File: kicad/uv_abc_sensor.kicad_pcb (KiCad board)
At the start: 2 copper layers, 25.4 x 17.8 mm, 23 parts, among them J1 Conn_01x04, J2 Conn_01x04, M1 MountingHole_2.5mm_Pad, M2 MountingHole_2.5mm_Pad, M3 MountingHole_2.5mm_Pad, M4 MountingHole_2.5mm_Pad, Q1 BSS138, Q2 BSS138, U1 AS7331, U2 AP2112K-3.3

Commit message: More work on layout.
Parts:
- moved C3 5.03 mm to (56.3, 55.8), turned to -90 degrees
- moved C4 2.55 mm to (59.3, 54.3), turned to 180 degrees
- moved U2 1.36 mm to (59.3, 56.8), turned to 0 degrees
- moved R7 0.51 mm to (61.2, 59.9)
- moved J1 0.13 mm to (53.5, 59.7)
- moved J2 0.13 mm to (73.6, 59.6)
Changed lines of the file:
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@@
   )
   (footprint "BOOMELE_SH_SMD:BOOMELE_SMD_SH_4PIN_RT" (layer "F.Cu")
-    (at 73.688 59.58 -90)
+    (at 73.561 59.58 -90)
     (property "Sheetfile" "uv_abc_sensor.kicad_sch")
     (property "Sheetname" "")
@@
   )
   (footprint "Capacitor_SMD:C_0402_1005Metric" (layer "F.Cu")
-    (at 61.534 55.4765 90)
+    (at 59.2755 54.29 180)
     (descr "Capacitor SMD 0402 (1005 Metric), square (rectangular) end terminal, IPC_7351 nominal, (Body size source: IPC-SM-782 page 76, https://www.pcb-3d.com/wordpress/wp-content/uploads/ipc-sm-782a_amendment_1_and_2.pdf), generated with kicad-footprint-generator")
     (tags "capacitor")
@@
     (property "ki_keywords" "cap capacitor")
     (attr smd)
-    (fp_text reference "C4" (at 0 -1.16 90) (layer "F.SilkS") hide
-        (effects (font (size 1 1) (thickness 0.15)))
-    )
-    (fp_text value "10uF" (at 0 1.16 90) (layer "F.Fab") hide
-        (effects (font (size 1 1) (thickness 0.15)))
-    )
-    (fp_text user "${REFERENCE}" (at 0 0 90) (layer "F.Fab")
+    (fp_text reference "C4" (at 0 -1.16) (layer "F.SilkS") hide
+        (effects (font (size 1 1) (thickness 0.15)))
+    )
+    (fp_text value "10uF" (at 0 1.16) (layer "F.Fab") hide
+        (effects (font (size 1 1) (thickness 0.15)))
+    )
+    (fp_text user "${REFERENCE}" (at 0 0) (layer "F.Fab")
         (effects (font (size 0.25 0.25) (thickness 0.04)))
     )
@@
     (fp_line (start 0.5 0.25) (end -0.5 0.25)
       (stroke (width 0.1) (type solid)) (layer "F.Fab"))
-    (pad "1" smd roundrect (at -0.48 0 90) (size 0.56 0.62) (layers "F.Cu" "F.Paste" "F.Mask") (roundrect_rratio 0.25)
+    (pad "1" smd roundrect (at -0.48 0 180) (size 0.56 0.62) (layers "F.Cu" "F.Paste" "F.Mask") (roundrect_rratio 0.25)
       (net 1 "+3.3V") (pintype "passive"))
-    (pad "2" smd roundrect (at 0.48 0 90) (size 0.56 0.62) (layers "F.Cu" "F.Paste" "F.Mask") (roundrect_rratio 0.25)
+    (pad "2" smd roundrect (at 0.48 0 180) (size 0.56 0.62) (layers "F.Cu" "F.Paste" "F.Mask") (roundrect_rratio 0.25)
       (net 2 "GND") (pintype "passive"))
     (model "${KICAD6_3DMODEL_DIR}/Capacitor_SMD.3dshapes/C_0402_1005Metric.wrl"
@@
   )
   (footprint "Resistor_SMD:R_0402_1005Metric" (layer "F.Cu")
-    (at 60.706 59.946 90)
+    (at 61.214 59.944 90)
     (descr "Resistor SMD 0402 (1005 Metric), square (rectangular) end terminal, IPC_7351 nominal, (Body size source: IPC-SM-782 page 72, https://www.pcb-3d.com/wordpress/wp-content/uploads/ipc-sm-782a_amendment_1_and_2.pdf), generated with kicad-footprint-generator")
     (tags "resistor")
@@
     (property "ki_keywords" "R res resistor")
     (attr smd)
-    (fp_text reference "R7" (at 0 -1.17 90) (layer "F.SilkS")
-        (effects (font (size 1 1) (thickness 0.15)))
-    )
-    (fp_text value "10k" (at 0 1.17 90) (layer "F.Fab")
+    (fp_text reference "R7" (at 0 -1.17 90) (layer "F.SilkS") hide
+        (effects (font (size 1 1) (thickness 0.15)))
+    )
+    (fp_text value "10k" (at 0 1.17 90) (layer "F.Fab") hide
         (effects (font (size 1 1) (thickness 0.15)))
     )
@@
   )
   (footprint "BOOMELE_SH_SMD:BOOMELE_SMD_SH_4PIN_RT" (layer "F.Cu")
-    (at 53.34 59.69 90)
+    (at 53.467 59.69 90)
     (property "Sheetfile" "uv_abc_sensor.kicad_sch")
     (property "Sheetname" "")
@@
   )
   (footprint "Capacitor_SMD:C_0402_1005Metric" (layer "F.Cu")
-    (at 59.982 52.4565 180)
+    (at 56.2555 55.842 -90)
     (descr "Capacitor SMD 0402 (1005 Metric), square (rectangular) end terminal, IPC_7351 nominal, (Body size source: IPC-SM-782 page 76, https://www.pcb-3d.com/wordpress/wp-content/uploads/ipc-sm-782a_amendment_1_and_2.pdf), generated with kicad-footprint-generator")
     (tags "capacitor")
@@
     (property "ki_keywords" "cap capacitor")
     (attr smd)
-    (fp_text reference "C3" (at 0 -1.16) (layer "F.SilkS") hide
-        (effects (font (size 1 1) (thickness 0.15)))
-    )
-    (fp_text value "10uF" (at 0 1.16) (layer "F.Fab") hide
-        (effects (font (size 1 1) (thickness 0.15)))
-    )
-    (fp_text user "${REFERENCE}" (at 0 0) (layer "F.Fab")
+    (fp_text reference "C3" (at 0 -1.16 -270) (layer "F.SilkS") hide
+        (effects (font (size 1 1) (thickness 0.15)))
+    )
+    (fp_text value "10uF" (at 0 1.16 -270) (layer "F.Fab") hide
+        (effects (font (size 1 1) (thickness 0.15)))
+    )
+    (fp_text user "${REFERENCE}" (at 0 0 -270) (layer "F.Fab")
         (effects (font (size 0.25 0.25) (thickness 0.04)))
     )
@@
     (fp_line (start 0.5 0.25) (end -0.5 0.25)
       (stroke (width 0.1) (type solid)) (layer "F.Fab"))
-    (pad "1" smd roundrect (at -0.48 0 180) (size 0.56 0.62) (layers "F.Cu" "F.Paste" "F.Mask") (roundrect_rratio 0.25)
+    (pad "1" smd roundrect (at -0.48 0 270) (size 0.56 0.62) (layers "F.Cu" "F.Paste" "F.Mask") (roundrect_rratio 0.25)
       (net 3 "VCC") (pintype "passive"))
-    (pad "2" smd roundrect (at 0.48 0 180) (size 0.56 0.62) (layers "F.Cu" "F.Paste" "F.Mask") (roundrect_rratio 0.25)
+    (pad "2" smd roundrect (at 0.48 0 270) (size 0.56 0.62) (layers "F.Cu" "F.Paste" "F.Mask") (roundrect_rratio 0.25)
       (net 2 "GND") (pintype "passive"))
     (model "${KICAD6_3DMODEL_DIR}/Capacitor_SMD.3dshapes/C_0402_1005Metric.wrl"
@@
   )
   (footprint "Package_TO_SOT_SMD:SOT-23-5" (layer "F.Cu")
-    (at 58.994 55.5045 -90)
+    (at 59.3035 56.83)
     (descr "SOT, 5 Pin (https://www.jedec.org/sites/default/files/docs/Mo-178c.PDF variant AA), generated with kicad-footprint-generator ipc_gullwing_generator.py")
     (tags "SOT TO_SOT_SMD")
@@
     (property "ki_keywords" "linear regulator ldo fixed positive")
     (attr smd)
-    (fp_text reference "U2" (at 0 -2.4 90) (layer "F.SilkS") hide
-        (effects (font (size 1 1) (thickness 0.15)))
-    )
-    (fp_text value "AP2112K-3.3" (at 0 2.4 90) (layer "F.Fab") hide
-        (effects (font (size 1 1) (thickness 0.15)))
-    )
-    (fp_text user "${REFERENCE}" (at 0 0 90) (layer "F.Fab")
+    (fp_text reference "U2" (at 0 -2.4) (layer "F.SilkS") hide
+        (effects (font (size 1 1) (thickness 0.15)))
+    )
+    (fp_text value "AP2112K-3.3" (at 0 2.4) (layer "F.Fab") hide
+        (effects (font (size 1 1) (thickness 0.15)))
+    )
+    (fp_text user "${REFERENCE}" (at 0 0) (layer "F.Fab")
         (effects (font (size 0.4 0.4) (thickness 0.06)))
     )
@@
     (fp_line (start 0.8 1.45) (end -0.8 1.45)
       (stroke (width 0.1) (type solid)) (layer "F.Fab"))
-    (pad "1" smd roundrect (at -1.1375 -0.95 270) (size 1.325 0.6) (layers "F.Cu" "F.Paste" "F.Mask") (roundrect_rratio 0.25)
+    (pad "1" smd roundrect (at -1.1375 -0.95) (size 1.325 0.6) (layers "F.Cu" "F.Paste" "F.Mask") (roundrect_rratio 0.25)
       (net 3 "VCC") (pinfunction "VIN") (pintype "power_in"))
-    (pad "2" smd roundrect (at -1.1375 0 270) (size 1.325 0.6) (layers "F.Cu" "F.Paste" "F.Mask") (roundrect_rratio 0.25)
+    (pad "2" smd roundrect (at -1.1375 0) (size 1.325 0.6) (layers "F.Cu" "F.Paste" "F.Mask") (roundrect_rratio 0.25)
       (net 2 "GND") (pinfunction "GND") (pintype "power_in"))
-    (pad "3" smd roundrect (at -1.1375 0.95 270) (size 1.325 0.6) (layers "F.Cu" "F.Paste" "F.Mask") (roundrect_rratio 0.25)
+    (pad "3" smd roundrect (at -1.1375 0.95) (size 1.325 0.6) (layers "F.Cu" "F.Paste" "F.Mask") (roundrect_rratio 0.25)
       (net 3 "VCC") (pinfunction "EN") (pintype "input"))
-    (pad "4" smd roundrect (at 1.1375 0.95 270) (size 1.325 0.6) (layers "F.Cu" "F.Paste" "F.Mask") (roundrect_rratio 0.25)
+    (pad "4" smd roundrect (at 1.1375 0.95) (size 1.325 0.6) (layers "F.Cu" "F.Paste" "F.Mask") (roundrect_rratio 0.25)
       (net 13 "unconnected-(U2-NC-Pad4)") (pinfunction "NC") (pintype "no_connect"))
-    (pad "5" smd roundrect (at 1.1375 -0.95 270) (size 1.325 0.6) (layers "F.Cu" "F.Paste" "F.Mask") (roundrect_rratio 0.25)
+    (pad "5" smd roundrect (at 1.1375 -0.95) (size 1.325 0.6) (layers "F.Cu" "F.Paste" "F.Mask") (roundrect_rratio 0.25)
       (net 1 "+3.3V") (pinfunction "VOUT") (pintype "power_out"))
     (model "${KICAD6_3DMODEL_DIR}/Package_TO_SOT_SMD.3dshapes/SOT-23-5.wrl"
@@
     (property "ki_keywords" "R res resistor")
     (attr smd)
-    (fp_text reference "R6" (at 0 -1.17) (layer "F.SilkS")
-        (effects (font (size 1 1) (thickness 0.15)))
-    )
-    (fp_text value "10k" (at 0 1.17) (layer "F.Fab")
-        (effects (font (size 1 1) (thickness 0.15)))
-    )
+    (fp_text reference "R6" (at 0 -1.17) (layer "F.SilkS") hide
+        (effects (font (size 1 1) (thickness 0.15)))
+    )
+    (fp_text value "10k" (at 0 1.17) (layer "F.Fab") hide
+        (effects (font (size 1 1) (thickness 0.15)))
+    )

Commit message: Worked on layout and routing.
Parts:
- moved C3 3.39 mm to (59.0, 57.9), turned to 0 degrees
- moved C4 2.45 mm to (56.9, 54.9), turned to -90 degrees
- moved U2 1.97 mm to (59.4, 54.9), turned to 90 degrees
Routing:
- net VCC: track 0.00 -> 37.4 mm, vias 0 -> 5
- net +3.3V: track 0.00 -> 31.9 mm
- net GND: track 0.00 -> 28.8 mm
- net /SCL_3V3: track 0.00 -> 2.05 mm
- net /SDA_3V3: track 0.00 -> 1.87 mm
- net Net-(U1-REXT): track 0.00 -> 1.73 mm
- net Net-(JP2-A): track 0.00 -> 1.45 mm
- net Net-(JP1-A): track 0.00 -> 1.23 mm

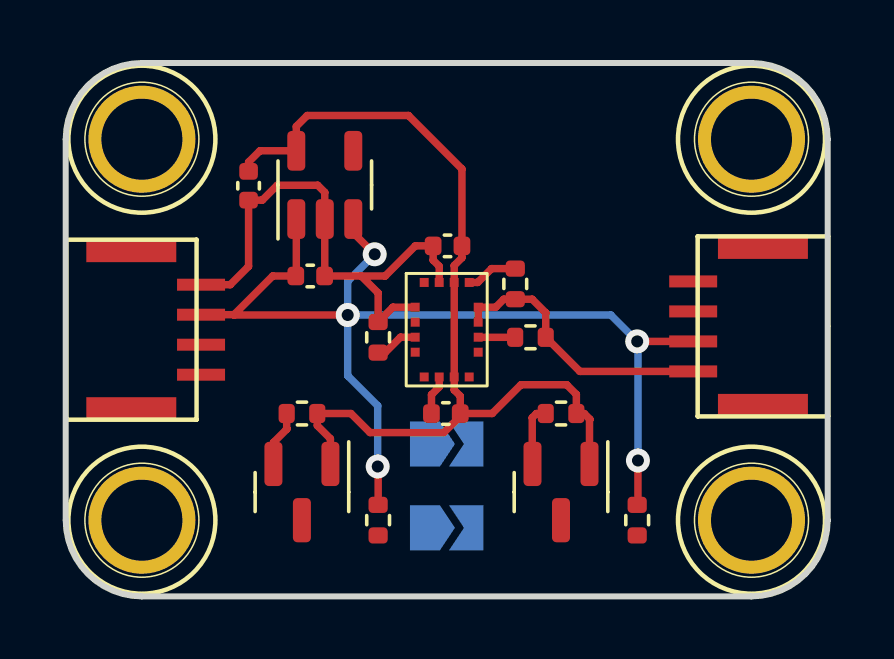
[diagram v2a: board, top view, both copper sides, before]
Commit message: Finished initial layout and routing.
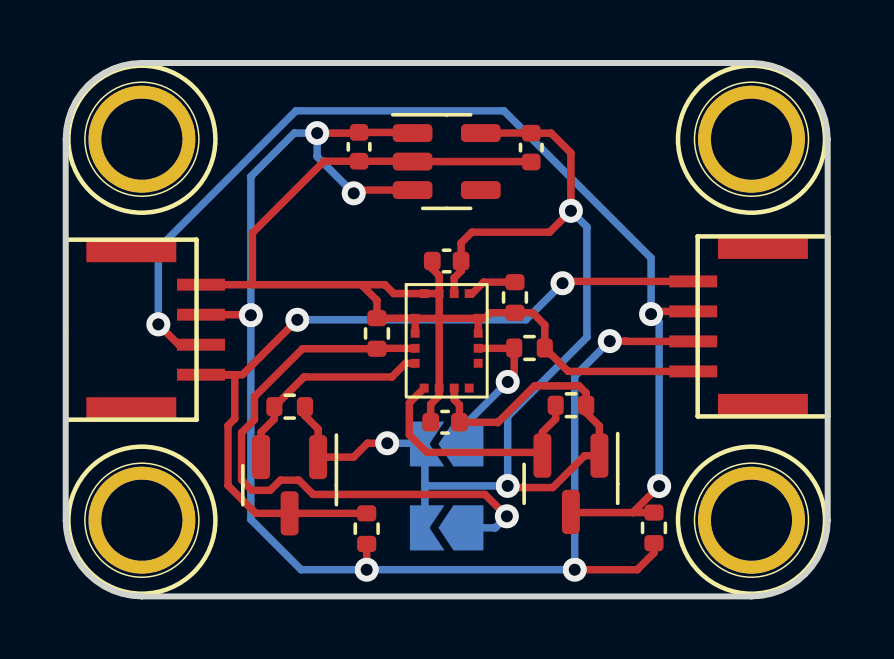
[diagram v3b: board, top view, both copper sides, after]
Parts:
- moved C4 9.51 mm to (66.3, 53.6)
- moved C3 4.60 mm to (60.6, 53.6), turned to -90 degrees
- moved U2 4.14 mm to (63.5, 54.1), turned to 0 degrees
- moved R3 0.62 mm to (70.4, 66.3), turned to 90 degrees
- moved C1 0.50 mm to (63.5, 57.4)
- moved R2 0.47 mm to (60.8, 66.3), turned to 90 degrees
- moved Q2 0.47 mm to (58.3, 64.9)
- moved R4 0.47 mm to (58.3, 62.3)
- moved R1 0.45 mm to (65.8, 58.6)
- moved R5 0.43 mm to (67.6, 62.2)
- moved Q1 0.43 mm to (67.6, 64.8)
- moved U1 0.37 mm to (63.5, 60.1)
- moved R6 0.36 mm to (66.3, 60.3)
- moved C2 0.29 mm to (63.4, 62.8)
- moved R7 0.13 mm to (61.2, 59.8)
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- renumbered Q2 to Q1, Q1 to Q2, R3 to R2, R2 to R3, R5 to R4, R4 to R5
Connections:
- Q1 pad 2: /SCL_3V3 -> /SDA_3V3
- Q1 pad 3: /SCL -> /SDA
- Q2 pad 2: /SDA_3V3 -> /SCL_3V3
- Q2 pad 3: /SDA -> /SCL
- R2 pad 2: /SDA -> /SCL
- R3 pad 2: /SCL -> /SDA
- R4 pad 2: /SDA_3V3 -> /SCL_3V3
- R5 pad 2: /SCL_3V3 -> /SDA_3V3
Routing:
- net /SDA: track 0.00 -> 37.8 mm, vias 0 -> 3
- net /SCL: track 0.00 -> 27.6 mm, vias 0 -> 2
- net Net-(JP2-A): track 1.45 -> 20.0 mm, vias 0 -> 1
- net +3.3V: track 31.9 -> 44.6 mm, vias 0 -> 3
- net VCC: track 37.4 -> 50.1 mm, vias 5 -> 6
- net GND: track 28.8 -> 39.9 mm
- net /SDA_3V3: track 1.87 -> 8.35 mm
- net /SCL_3V3: track 2.05 -> 7.16 mm
- net Net-(JP1-A): track 1.23 -> 5.04 mm, vias 0 -> 1

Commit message: Added production files.
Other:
- board text added: "AS7331 UV ABC Sensor V0.1 R1 www.iorodeo.com"
- board text removed: "AS7331 UV ABC Sensor www.iorodeo.com"
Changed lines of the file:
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@@
       (outputformat 1)
       (mirror false)
-      (drillshape 1)
+      (drillshape 0)
       (scaleselection 1)
-      (outputdirectory "")
+      (outputdirectory "production/rev1/gerber/")
     )
   )
@@
   (gr_line (start 53.34 50.8) (end 73.66 50.8)
     (stroke (width 0.2) (type default)) (layer "Edge.Cuts"))
-  (gr_text "AS7331 \nUV ABC Sensor \nwww.iorodeo.com\n" (at 63.5 57.15) (layer "B.SilkS")
+  (gr_text "AS7331 \nUV ABC Sensor \nV0.1 R1\nwww.iorodeo.com\n" (at 63.5 57.658) (layer "B.SilkS")
     (effects (font (size 1 1) (thickness 0.15)) (justify bottom mirror))
   )

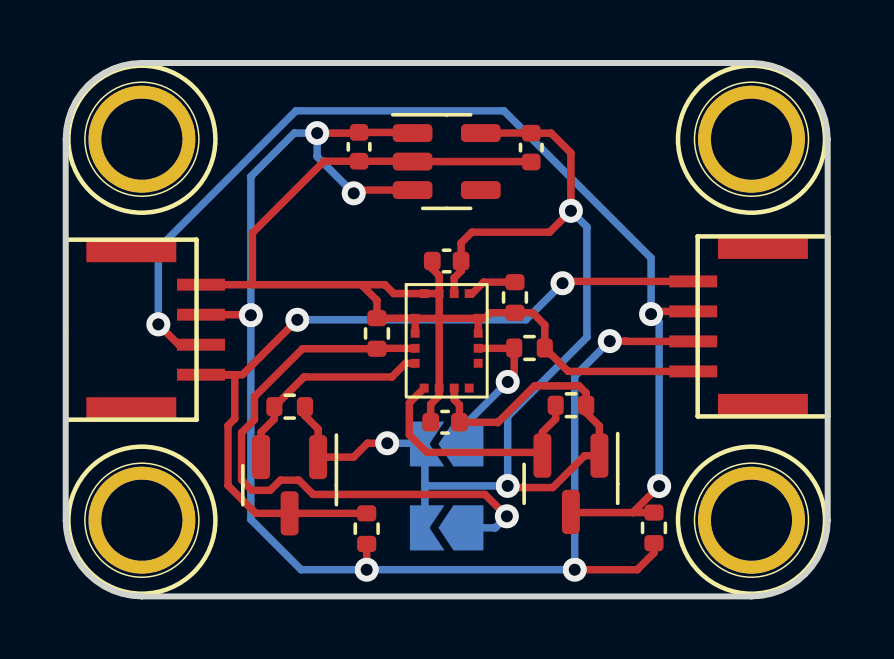
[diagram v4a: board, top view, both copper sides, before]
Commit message: Completed v0.1 rev2 of the sensor design.
Modified as7331 footprint to (hopefully) descrease error rate.  Made
pads slightly larger. Also, removed all traces directly under the IC.
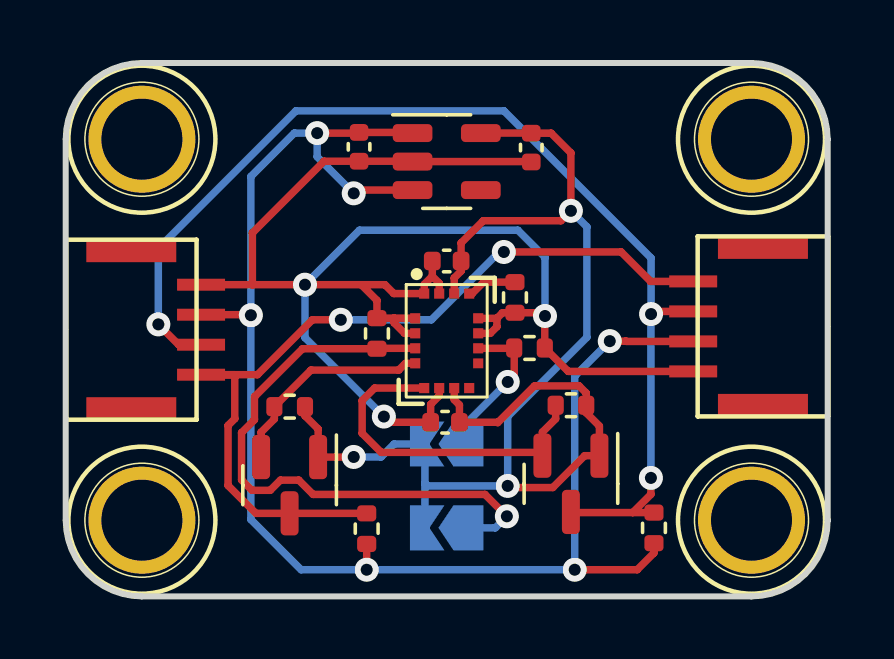
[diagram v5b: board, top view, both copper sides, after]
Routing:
- net GND: track 39.9 -> 54.2 mm, vias 0 -> 3
- net /SDA_3V3: track 8.35 -> 11.5 mm
- net /SCL: track 27.6 -> 28.4 mm
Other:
- board text added: "AS7331 UV ABC Sensor V0.1 R2 www.iorodeo.com"
- board text removed: "AS7331 UV ABC Sensor V0.1 R1 www.iorodeo.com"
